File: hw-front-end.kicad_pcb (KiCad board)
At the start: 2 copper layers, 165 x 65 mm, 75 parts, among them J102 DSUB-25, J201 Conn_01x08_Pin, J202 Conn_01x08_Pin, J301 Conn_01x12_Pin, J302 Conn_01x12_Pin, J303 Conn_01x12_Pin, J304 Conn_01x12_Pin, U101 USBLC6-4SC6, U102 USBLC6-4SC6, U103 USBLC6-4SC6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

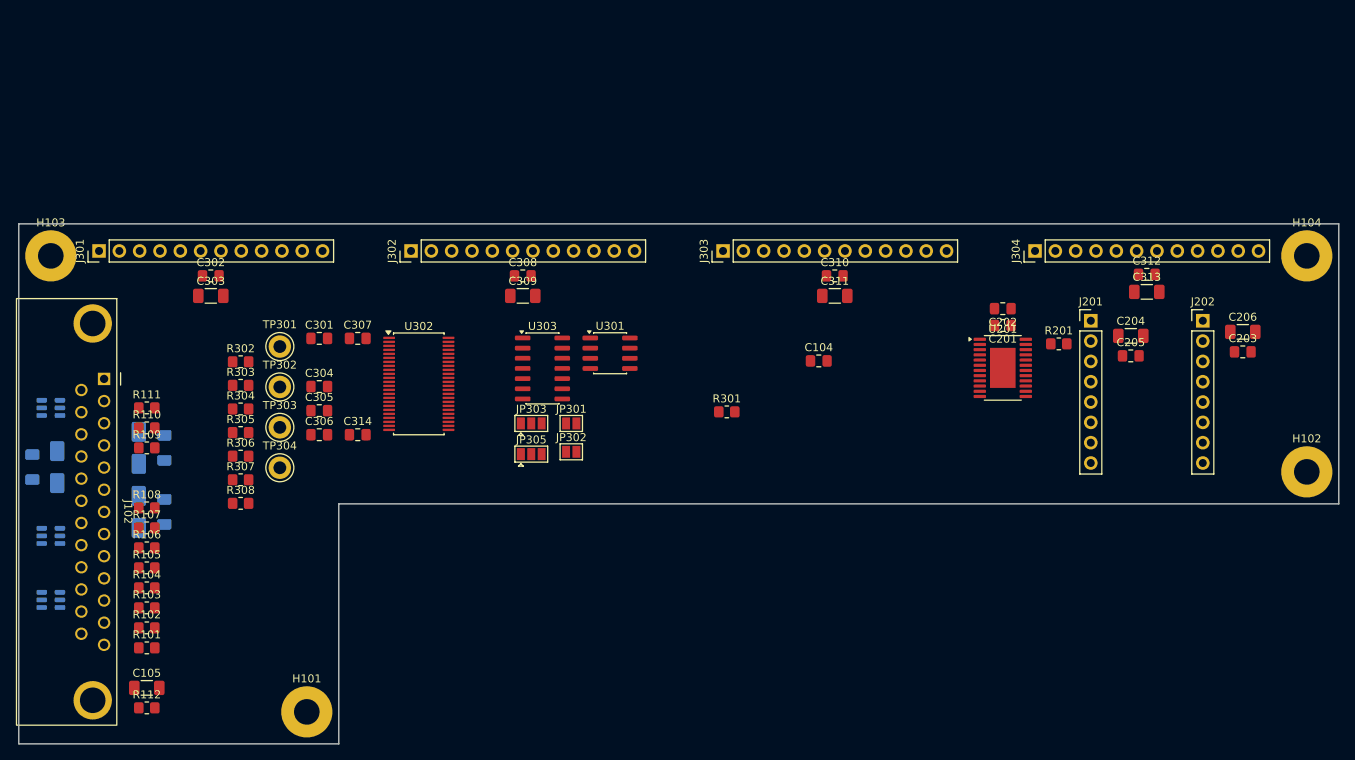
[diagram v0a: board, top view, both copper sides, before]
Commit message: Most tracks routed
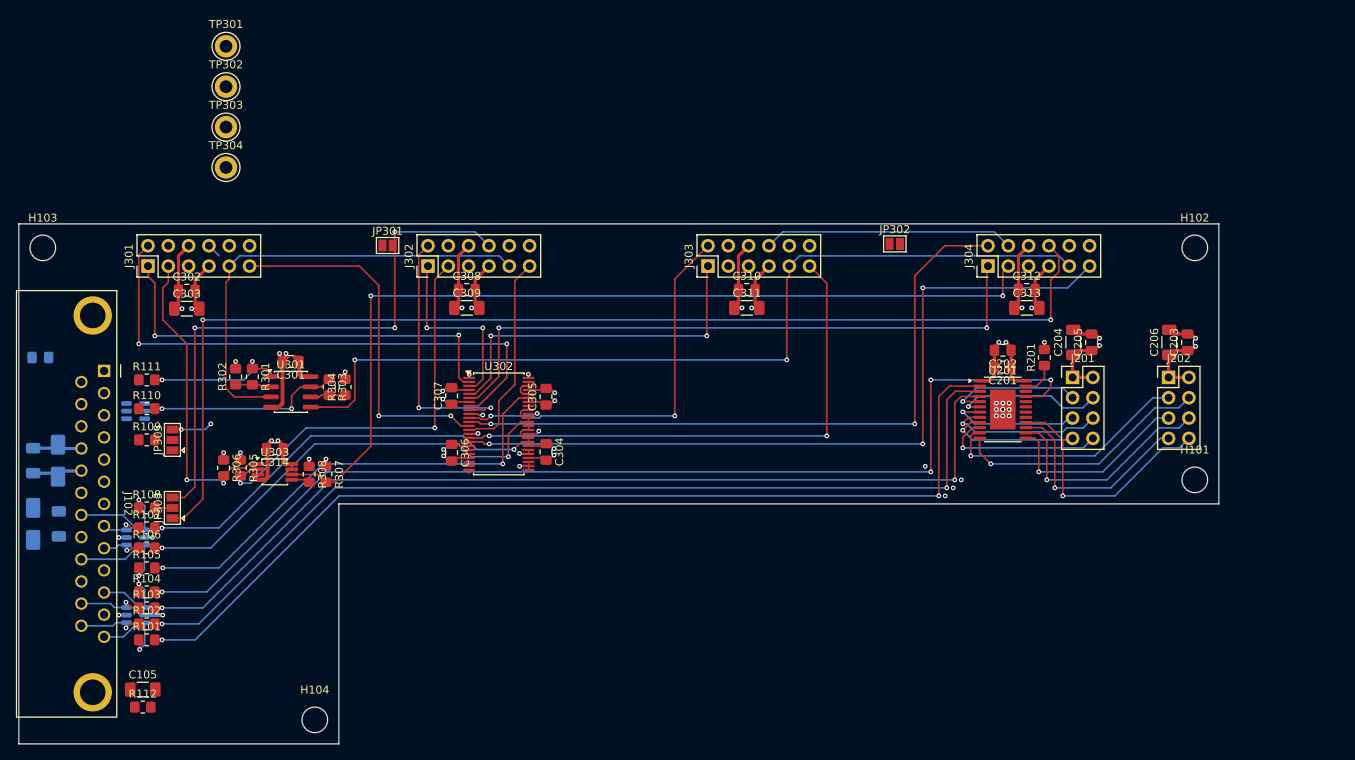
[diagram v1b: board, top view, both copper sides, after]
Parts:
- removed C103: 10u, Capacitor_SMD:C_1206_3216Metric_Pad1.33x1.80mm_HandSolder
- removed D103: SMAJ5.0A, Diode_SMD:D_SMA
- C104: moved to B.Cu
- H101, H102, H103, H104: value MountingHole_Pad -> MountingHole; footprint MountingHole:MountingHole_3.2mm_M3_Pad -> MountingHole:MountingHole_3.2mm_M3_DIN965
- J201, J202: footprint Connector_PinHeader_2.54mm:PinHeader_1x08_P2.54mm_Vertical -> Connector_PinHeader_2.54mm:PinHeader_2x04_P2.54mm_Vertical
- J301, J302, J303, J304: footprint Connector_PinHeader_2.54mm:PinHeader_1x12_P2.54mm_Vertical -> Connector_PinHeader_2.54mm:PinHeader_2x06_P2.54mm_Vertical
- U303: value SN74LVC32A -> 74LVC2G32; footprint Package_SO:SOIC-14_3.9x8.7mm_P1.27mm -> Package_SO:VSSOP-8_3x3mm_P0.65mm
- moved H104 136.9 mm to (137.0, 147.0)
- moved H101 114.7 mm to (247.0, 117.0)
- moved C104 97.3 mm to (102.7, 101.7), turned to 180 degrees
- moved R301 59.5 mm to (129.2, 104.1), turned to -90 degrees
- moved JP302 48.1 mm to (209.5, 87.5)
- moved JP303 46.1 mm to (119.2, 120.5), turned to 90 degrees
- moved JP305 44.9 mm to (119.2, 112.0), turned to 90 degrees
- moved U301 40.2 mm to (134.0, 106.0)
- moved TP302 38.1 mm to (125.9, 67.8)
- moved TP301 38.1 mm to (125.9, 62.8)
- moved TP303 38.1 mm to (125.9, 72.9)
- moved TP304 38.1 mm to (125.9, 78.0)
- moved U303 35.9 mm to (132.0, 116.0)
- moved JP301 32.0 mm to (146.1, 87.7)
- moved H102 31.3 mm to (247.0, 88.0)
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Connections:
- C102 pad 1: +3V3A -> +3V3
- D102 pad 1: +3V3A -> +3V3
- J102 pad 10: Net-(U103-I/O4) -> GND
- J102 pad 11: Net-(U101-I/O1) -> Net-(U101-I/O3)
- J102 pad 18: +3V3A -> +3V3
- J102 pad 22: GND -> Net-(J102-P22)
- J102 pad 9: Net-(U103-I/O3) -> Net-(U103-I/O1)
- R104 pad 1: Net-(U101-I/O1) -> Net-(U101-I/O3)
- R105 pad 1: Net-(U103-I/O4) -> Net-(J102-P22)
- R106 pad 1: Net-(U103-I/O3) -> Net-(U103-I/O1)
- R107 pad 2: /Photodiode Array Interface/S13886_CTRL.VIDEO_34 -> /Photodiode Array Interface/S13886_CTRL.GAIN
- R110 pad 2: /Photodiode Array Interface/S13886_CTRL.GAIN -> /Photodiode Array Interface/S13886_CTRL.VIDEO_34
- U101 pad 1: Net-(U101-I/O1) -> Net-(J102-P25)
- U101 pad 4: Net-(J102-P25) -> Net-(U101-I/O3)
- U103 pad 1: Net-(J102-P20) -> Net-(U103-I/O1)
- U103 pad 4: Net-(U103-I/O3) -> Net-(J102-P20)
- U103 pad 6: Net-(U103-I/O4) -> Net-(J102-P22)
- U303 pad 3: Net-(JP305-B) -> Net-(JP305-A)
- U303 pad 4: /Photodiode Array Interface/S13886.TRG_3 -> GND
- U303 pad 5: /Photodiode Array Interface/S13886.TRG_4 -> /Photodiode Array Interface/S13886.TRG_3
- U303 pad 6: Net-(JP305-A) -> /Photodiode Array Interface/S13886.TRG_4
- U303 pad 7: GND -> Net-(JP305-B)
- U303 pad 8: (no net) -> +3V3
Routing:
- net /Photodiode Array Interface/S13886.EOS_4: track 0.00 -> 143.4 mm, vias 0 -> 2
- net /LED Driver/LED_SERIAL.~{OE}: track 0.00 -> 134.3 mm, vias 0 -> 4
- net /LED Driver/LED_SERIAL.DATA: track 0.00 -> 123.5 mm, vias 0 -> 2
- net /LED Driver/LED_SERIAL.SCK: track 0.00 -> 121.6 mm, vias 0 -> 2
- net /LED Driver/LED_SERIAL.LE: track 0.00 -> 119.7 mm, vias 0 -> 2
- net /Photodiode Array Interface/S13886.VIDEO_34: track 0.00 -> 114.1 mm, vias 0 -> 2
- net /Photodiode Array Interface/S13886.TRG_4: track 0.00 -> 114.0 mm, vias 0 -> 2
- net /Photodiode Array Interface/S13886.GAIN_4: track 0.00 -> 98.3 mm, vias 0 -> 3
- net GND: track 0.00 -> 96.9 mm, vias 0 -> 46
- net /Photodiode Array Interface/S13886.CLK_4: track 0.00 -> 85.0 mm, vias 0 -> 2
- net /Photodiode Array Interface/S13886.RST_4: track 0.00 -> 79.7 mm, vias 0 -> 2
- net +3V3: track 0.00 -> 77.1 mm, vias 0 -> 12
- net /Photodiode Array Interface/S13886.EOS_2: track 0.00 -> 72.9 mm, vias 0 -> 3
- net /Photodiode Array Interface/S13886.CLK_1: track 0.00 -> 69.1 mm, vias 0 -> 2
- net /Photodiode Array Interface/S13886.GAIN_3: track 0.00 -> 66.9 mm, vias 0 -> 2
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- added copper zone on In2.Cu, net +3V3
- added copper zone on In1.Cu, net GND
- added copper zone on In4.Cu, net GND
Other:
- board size 165 x 65 mm -> 150 x 65 mm
- copper layers 2 -> 6

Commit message: DRC clean
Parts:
- R112: footprint Resistor_SMD:R_0805_2012Metric_Pad1.20x1.40mm_HandSolder -> Resistor_SMD:R_1206_3216Metric_Pad1.30x1.75mm_HandSolder
- moved TP304 93.8 mm to (217.0, 100.4)
- moved TP302 49.1 mm to (116.3, 116.0)
- moved TP301 43.2 mm to (119.7, 105.6)
- moved TP303 26.3 mm to (142.9, 93.0)
- moved JP302 6.50 mm to (216.0, 87.7)
- moved C104 5.41 mm to (105.7, 106.2), turned to -90 degrees
- moved C101 3.24 mm to (101.8, 122.0)
- moved D101 3.14 mm to (104.9, 122.0)
- moved R111 1.50 mm to (116.0, 103.0)
- moved R306 1.22 mm to (125.8, 114.3)
- moved R305 1.20 mm to (127.8, 114.3)
- moved JP301 1.20 mm to (146.1, 88.9)
- moved R112 0.20 mm to (115.5, 145.6)
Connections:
- net Net-(JP305-A) renamed /Photodiode Array Interface/TRG_34
- net Net-(JP305-B) renamed /Photodiode Array Interface/TRG_12
- C105 pad 1: Net-(C105-Pad1) -> /CHASSIS
- J102 pad 2: Net-(U102-I/O1) -> Net-(U102-I/O4)
- J102 pad 3: Net-(U102-I/O2) -> Net-(U102-I/O3)
- J102 pad 4: Net-(U102-I/O3) -> Net-(U102-I/O2)
- J102 pad S1: Net-(C105-Pad1) -> unconnected-(J102-SHIELD-PadS1)
- J102 pad S2: Net-(C105-Pad1) -> /CHASSIS
- R109 pad 1: Net-(U102-I/O3) -> Net-(U102-I/O2)
- R110 pad 1: Net-(U102-I/O2) -> Net-(U102-I/O3)
- R111 pad 1: Net-(U102-I/O1) -> Net-(U102-I/O4)
- R112 pad 1: Net-(C105-Pad1) -> /CHASSIS
- U102 pad 1: Net-(U102-I/O1) -> +2V5
- U102 pad 6: +2V5 -> Net-(U102-I/O4)
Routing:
- net +2V5: track 0.00 -> 159.5 mm
- net +12V: track 18.3 -> 172.5 mm
- net /Photodiode Array Interface/S13886.TRG_3: track 2.32 -> 78.8 mm, vias 0 -> 1
- net /Photodiode Array Interface/EOS_1: track 1.79 -> 36.0 mm, vias 0 -> 2
- net /Photodiode Array Interface/TRG_12: track 5.09 -> 27.1 mm
- net /Photodiode Array Interface/TRG_34: track 0.00 -> 16.4 mm, vias 0 -> 2
- net GND: track 96.9 -> 109.8 mm, vias 46 -> 50
- net /Photodiode Array Interface/S13886.EOS_4: track 143.4 -> 154.2 mm, vias 2 -> 4
- net Net-(U102-I/O2): track 0.00 -> 9.00 mm, vias 0 -> 1
- net Net-(U102-I/O4): track 0.00 -> 8.43 mm, vias 0 -> 1
- net Net-(U102-I/O3): track 0.00 -> 7.24 mm, vias 0 -> 1
- net /Photodiode Array Interface/S13886.EOS_2: track 72.9 -> 79.7 mm, vias 3 -> 4
- net /Photodiode Array Interface/EOS_3: track 31.4 -> 38.0 mm, vias 0 -> 2
- net +3V3: track 77.1 -> 79.4 mm, vias 12 -> 20
- net /Photodiode Array Interface/S13886_CTRL.TRG: track 0.00 -> 2.20 mm
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- added copper zone on B.Cu, net +3V3
- added copper zone on F.Cu, net /CHASSIS
- added copper zone on F.Cu, net GND

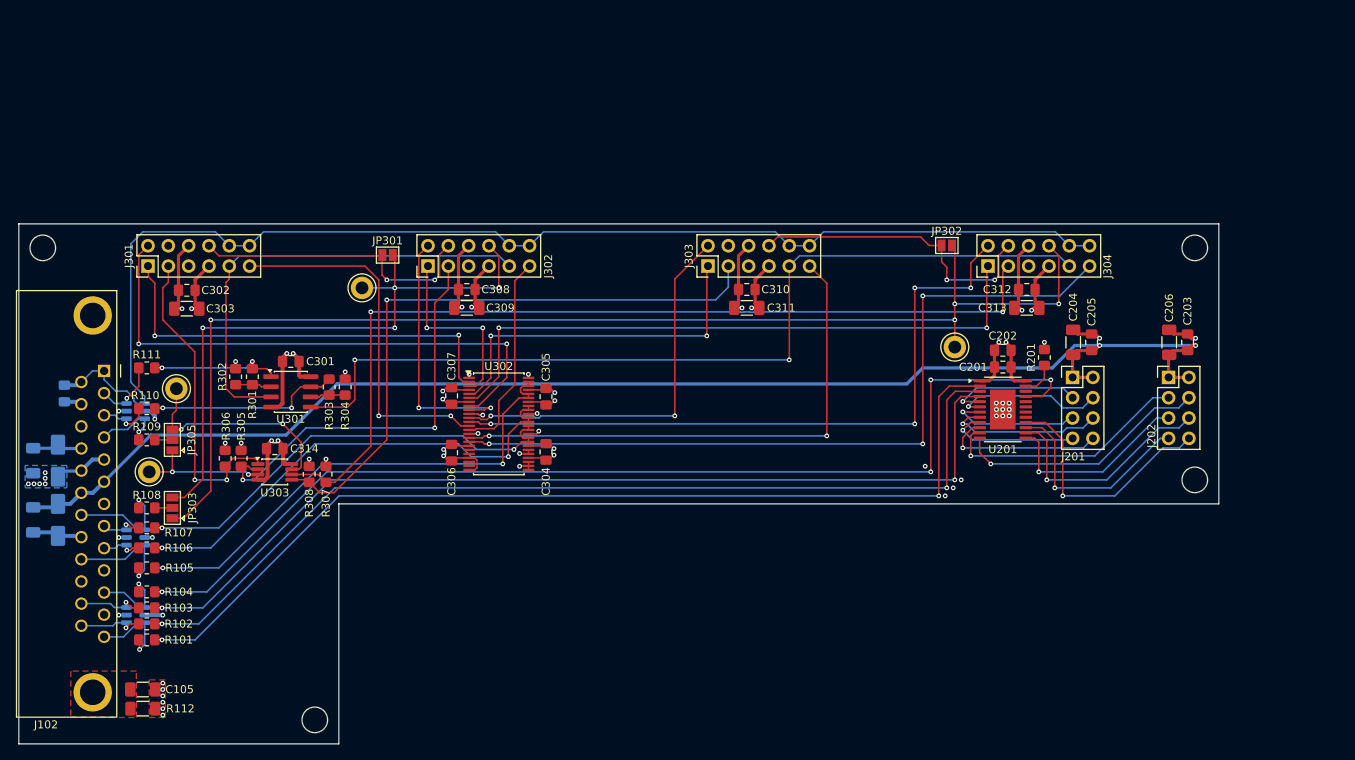
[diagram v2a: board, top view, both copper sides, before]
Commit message: added stitching vias and silkscreen
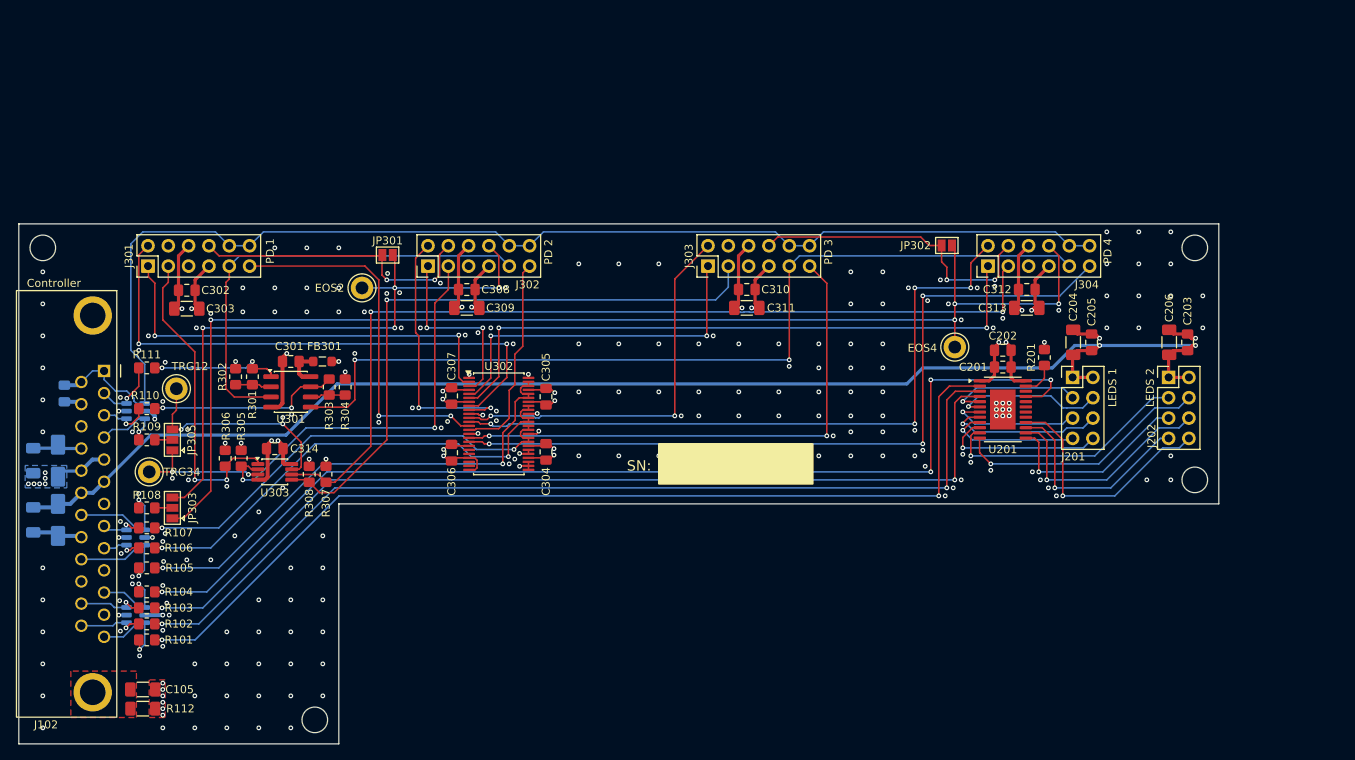
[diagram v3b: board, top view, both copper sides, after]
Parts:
- added FB301: 220R@100MHz, Inductor_SMD:L_0805_2012Metric_Pad1.05x1.20mm_HandSolder, F.Cu at (138.0, 102.2)
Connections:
- C301 pad 1: +3V3 -> Net-(U301C-V+)
- U301 pad 8: +3V3 -> Net-(U301C-V+)
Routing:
- net Net-(U301C-V+): track 0.00 -> 5.15 mm
- net +3V3: track 79.4 -> 75.8 mm
- net GND: vias 50 -> 239
- added copper zone on In3.Cu, net +3V3
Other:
- board text added: "Controller"
- board text added: "EOS2"
- board text added: "EOS4"
- board text added: "LEDS 1"
- board text added: "LEDS 2"
- board text added: "PD 1"
- board text added: "PD 2"
- board text added: "PD 3"
- board text added: "PD 4"
- board text added: "SN:"
- board text added: "TRG12"
- board text added: "TRG34"

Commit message: minor changes
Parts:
- J201, J202: value Conn_01x08_Pin -> Conn_02x04_Pin
- J301, J302, J303, J304: value Conn_01x12_Pin -> Conn_02x06_Pin
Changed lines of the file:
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@@
 			)
 		)
-		(property "Value" "Conn_01x12_Pin"
+		(property "Value" "Conn_02x06_Pin"
 			(at 1.27 15.08 90)
 			(layer "F.Fab")
@@
 			)
 		)
-		(property "Description" "CONN HEADER R/A 12POS 2.54MM"
+		(property "Description" "CONN HEADER VERTICAL 12POS 2.54MM"
 			(at 0 0 90)
 			(layer "F.Fab")
@@
 			)
 		)
-		(property "MPN" ""
+		(property "MPN" "G800W590018EU"
 			(at 0 0 90)
 			(unlocked yes)
@@
 			)
 		)
-		(property "Manufacturer" ""
+		(property "Manufacturer" "Amphenol ICC"
 			(at 0 0 90)
 			(unlocked yes)
@@
 			)
 		)
-		(property "Value" "Conn_01x12_Pin"
+		(property "Value" "Conn_02x06_Pin"
 			(at 1.27 15.08 90)
 			(layer "F.Fab")
@@
 			)
 		)
-		(property "Description" "CONN HEADER R/A 12POS 2.54MM"
+		(property "Description" "CONN HEADER VERTICAL 12POS 2.54MM"
 			(at 0 0 90)
 			(layer "F.Fab")
@@
 			)
 		)
-		(property "MPN" ""
+		(property "MPN" "G800W590018EU"
 			(at 0 0 90)
 			(unlocked yes)
@@
 			)
 		)
-		(property "Manufacturer" ""
+		(property "Manufacturer" "Amphenol ICC"
 			(at 0 0 90)
 			(unlocked yes)
@@
 			)
 		)
-		(property "MPN" " OPA350UA/2K5"
+		(property "MPN" "OPA350UA/2K5"
 			(at 0 0 0)
 			(unlocked yes)
@@
 			)
 		)
-		(property "Description" ""
+		(property "Description" "CAP CER 1UF 10V X7R 0805"
 			(at 0 0 0)
 			(layer "F.Fab")
@@
 			)
 		)
-		(property "Value" "Conn_01x12_Pin"
+		(property "Value" "Conn_02x06_Pin"
 			(at 1.27 15.08 90)
 			(layer "F.Fab")
@@
 			)
 		)
-		(property "Description" "CONN HEADER R/A 12POS 2.54MM"
+		(property "Description" "CONN HEADER VERTICAL 12POS 2.54MM"
 			(at 0 0 90)
 			(layer "F.Fab")
@@
 			)
 		)
-		(property "MPN" ""
+		(property "MPN" "G800W590018EU"
 			(at 0 0 90)
 			(unlocked yes)
@@
 			)
 		)
-		(property "Manufacturer" ""
+		(property "Manufacturer" "Amphenol ICC"
 			(at 0 0 90)
 			(unlocked yes)
@@
 			)
 		)
-		(property "Manufacturer" "Texas Instrument"
+		(property "Manufacturer" "Texas Instruments"
 			(at 0 0 0)
 			(unlocked yes)
@@
 			)
 		)
-		(property "Value" "Conn_01x08_Pin"
+		(property "Value" "Conn_02x04_Pin"
 			(at 1.27 10 0)
 			(layer "F.Fab")
@@
 			)
 		)
-		(property "Description" "CONN HEADER R/A 8POS 2.54MM"
+		(property "Description" "CONN HEADER VERTICAL 8POS 2.54MM"
 			(at 0 0 0)
 			(layer "F.Fab")
@@
 			)
 		)
-		(property "MPN" ""
+		(property "MPN" "PR20204VBDN"
 			(at 0 0 0)
 			(unlocked yes)
@@
 			)
 		)
-		(property "Manufacturer" ""
+		(property "Manufacturer" "METZ CONNECT"
 			(at 0 0 0)
 			(unlocked yes)
@@
 			)
 		)
-		(property "Manufacturer" "Würth Elektronik"
+		(property "Manufacturer" "Wurth Elektronik"
 			(at 0 0 270)
 			(unlocked yes)
@@
 			)
 		)
-		(property "Value" "Conn_01x12_Pin"
+		(property "Value" "Conn_02x06_Pin"
 			(at 1.27 15.08 90)
 			(layer "F.Fab")
@@
 			)
 		)
-		(property "Description" "CONN HEADER R/A 12POS 2.54MM"
+		(property "Description" "CONN HEADER VERTICAL 12POS 2.54MM"
 			(at 0 0 90)
 			(layer "F.Fab")
@@
 			)
 		)
-		(property "MPN" ""
+		(property "MPN" "G800W590018EU"
 			(at 0 0 90)
 			(unlocked yes)
@@
 			)
 		)
-		(property "Manufacturer" ""
+		(property "Manufacturer" "Amphenol ICC"
 			(at 0 0 90)
 			(unlocked yes)
@@
 			)
 		)
-		(property "Value" "Conn_01x08_Pin"
+		(property "Value" "Conn_02x04_Pin"
 			(at 1.27 10 0)
 			(layer "F.Fab")
@@
 			)
 		)
-		(property "Description" "CONN HEADER R/A 8POS 2.54MM"
+		(property "Description" "CONN HEADER VERTICAL 8POS 2.54MM"
 			(at 0 0 0)
 			(layer "F.Fab")
@@
 			)
 		)
-		(property "MPN" ""
+		(property "MPN" "PR20204VBDN"
 			(at 0 0 0)
 			(unlocked yes)
@@
 			)
 		)
-		(property "Manufacturer" ""
+		(property "Manufacturer" "METZ CONNECT"
 			(at 0 0 0)
 			(unlocked yes)
@@
 			)
 		)
-		(property "Manufacturer" "Texas Instrument"
+		(property "Manufacturer" "Texas Instruments"
 			(at 0 0 0)
 			(unlocked yes)
@@
 			)
 		)
-		(property "Manufacturer" "Littlefuse"
+		(property "Manufacturer" "Littelfuse"
 			(at 0 0 90)
 			(unlocked yes)
@@
 			)
 		)
-		(property "Manufacturer" "Littlefuse"
+		(property "Manufacturer" "Littelfuse"
 			(at 0 0 270)
 			(unlocked yes)
@@
 	)
 	(segment
+		(start 136.805 102.2)
+		(end 135.0375 102.2)
+		(width 0.5)
+		(layer "F.Cu")
+		(net "Net-(U301C-V+)")
+	)
+	(segment
+		(start 135.395 104.095)
+		(end 135.0375 103.7375)
+		(width 0.5)
+		(layer "F.Cu")
+		(net "Net-(U301C-V+)")
+	)
+	(segment
+		(start 135.0375 102.2)
+		(end 135.0375 101.9375)
+		(width 0.5)
+		(layer "F.Cu")
+		(net "Net-(U301C-V+)")
+	)
+	(segment
+		(start 135.0375 103.7375)
+		(end 135.0375 102.2)
+		(width 0.5)
+		(layer "F.Cu")
+		(net "Net-(U301C-V+)")
+	)
+	(segment
+		(start 136.475 104.095)
+		(end 135.395 104.095)
+		(width 0.5)
+		(layer "F.Cu")
+		(net "Net-(U301C-V+)")
+	)
+	(segment
 		(start 215 119)
 		(end 215 106.6)
@@
 		(net "Net-(J102-P24)")
 	)
-	(segment
-		(start 136.805 102.2)
-		(end 135.0375 102.2)
-		(width 0.5)
-		(layer "F.Cu")
-		(net "Net-(U301C-V+)")
-	)
-	(segment
-		(start 135.395 104.095)
-		(end 135.0375 103.7375)
-		(width 0.5)
-		(layer "F.Cu")
-		(net "Net-(U301C-V+)")
-	)
-	(segment
-		(start 135.0375 102.2)
-		(end 135.0375 101.9375)
-		(width 0.5)
-		(layer "F.Cu")
-		(net "Net-(U301C-V+)")
-	)
-	(segment
-		(start 135.0375 103.7375)
-		(end 135.0375 102.2)
-		(width 0.5)
-		(layer "F.Cu")
-		(net "Net-(U301C-V+)")
-	)
-	(segment
-		(start 136.475 104.095)
-		(end 135.395 104.095)
-		(width 0.5)
-		(layer "F.Cu")
-		(net "Net-(U301C-V+)")
-	)
 	(zone
